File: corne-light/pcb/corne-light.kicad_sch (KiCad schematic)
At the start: 92 parts, among them J1 MJ-4PP-9, J2 OLED, J6 MJ-4PP-9, J7 OLED, SW1 SW_PUSH, SW10 SW_PUSH, SW11 SW_PUSH, SW12 SW_PUSH, SW13 SW_PUSH, SW14 SW_PUSH, SW15 SW_PUSH, SW16 SW_PUSH, SW17 SW_PUSH, SW18 SW_PUSH, SW19 SW_PUSH, SW2 SW_PUSH, SW20 SW_PUSH, SW21 SW_PUSH, SW22 SW_PUSH, SW23 SW_PUSH, SW24 SW_PUSH, SW25 SW_PUSH, SW26 SW_PUSH, SW27 SW_PUSH, SW28 SW_PUSH, SW29 SW_PUSH, SW3 SW_PUSH, SW30 SW_PUSH, SW31 SW_PUSH, SW32 SW_PUSH, SW33 SW_PUSH, SW34 SW_PUSH, SW35 SW_PUSH, SW36 SW_PUSH, SW37 SW_PUSH, SW38 SW_PUSH, SW39 SW_PUSH, SW4 SW_PUSH, SW40 SW_PUSH, SW41 SW_PUSH, SW42 SW_PUSH, SW5 SW_PUSH, SW6 SW_PUSH, SW7 SW_PUSH, SW8 SW_PUSH, SW9 SW_PUSH, U1 ProMicro, U2 ProMicro

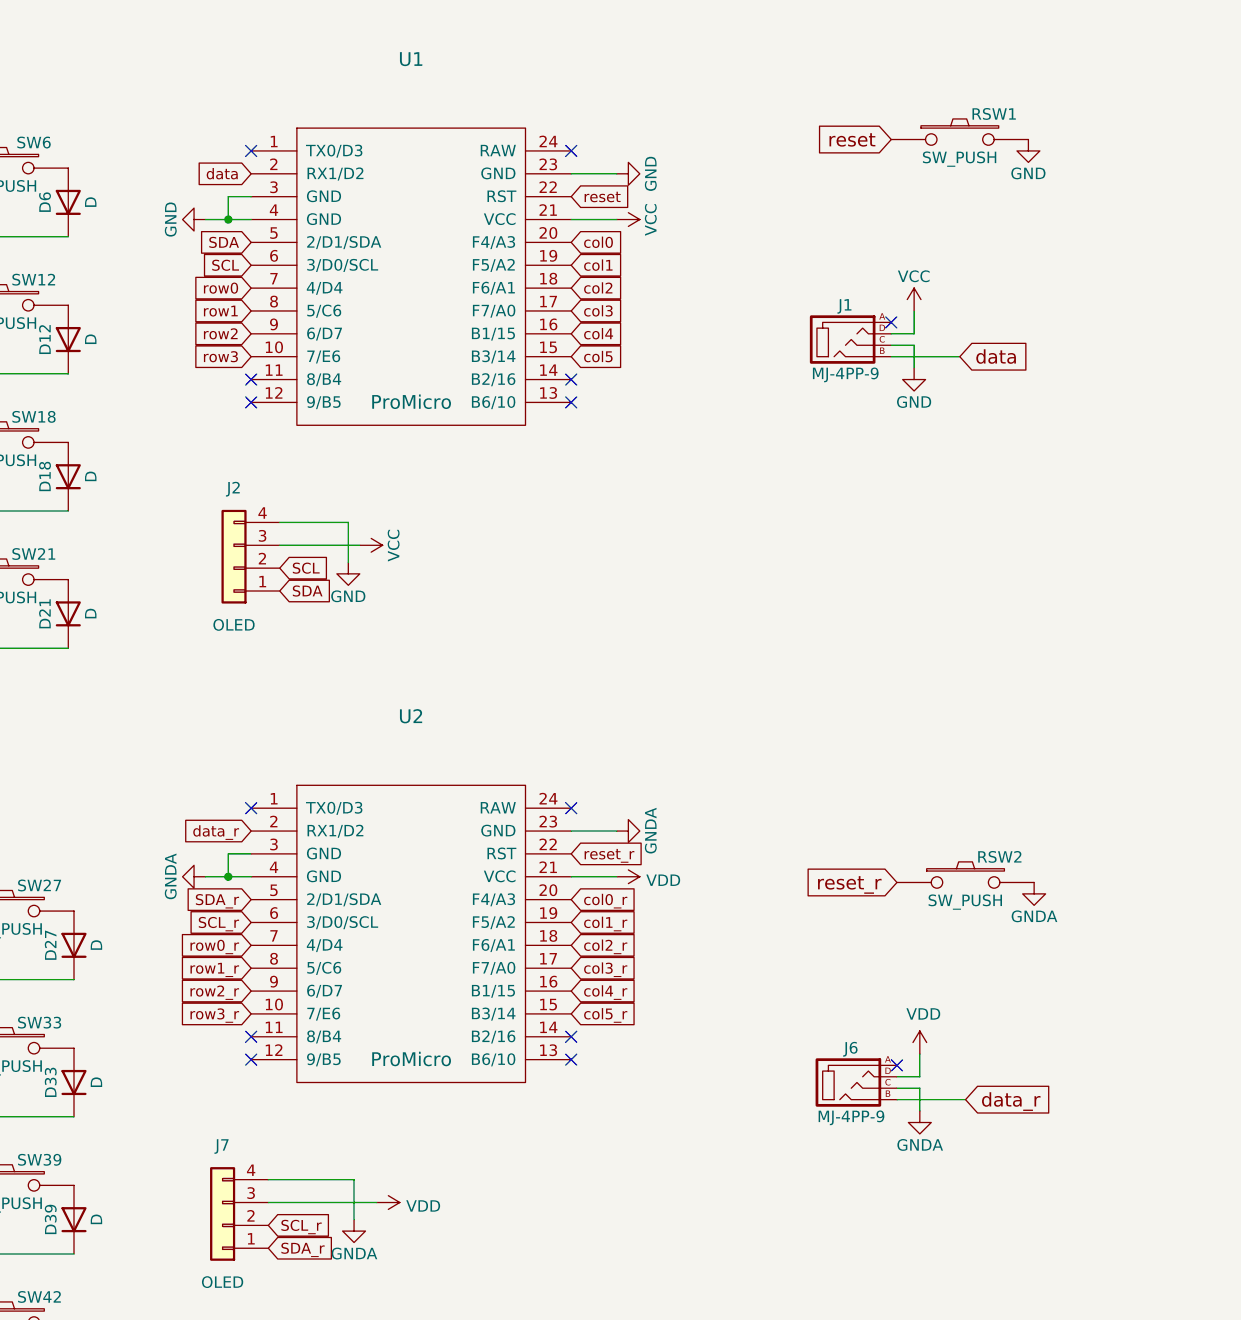
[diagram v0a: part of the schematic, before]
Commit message: Change switches to redragon ones
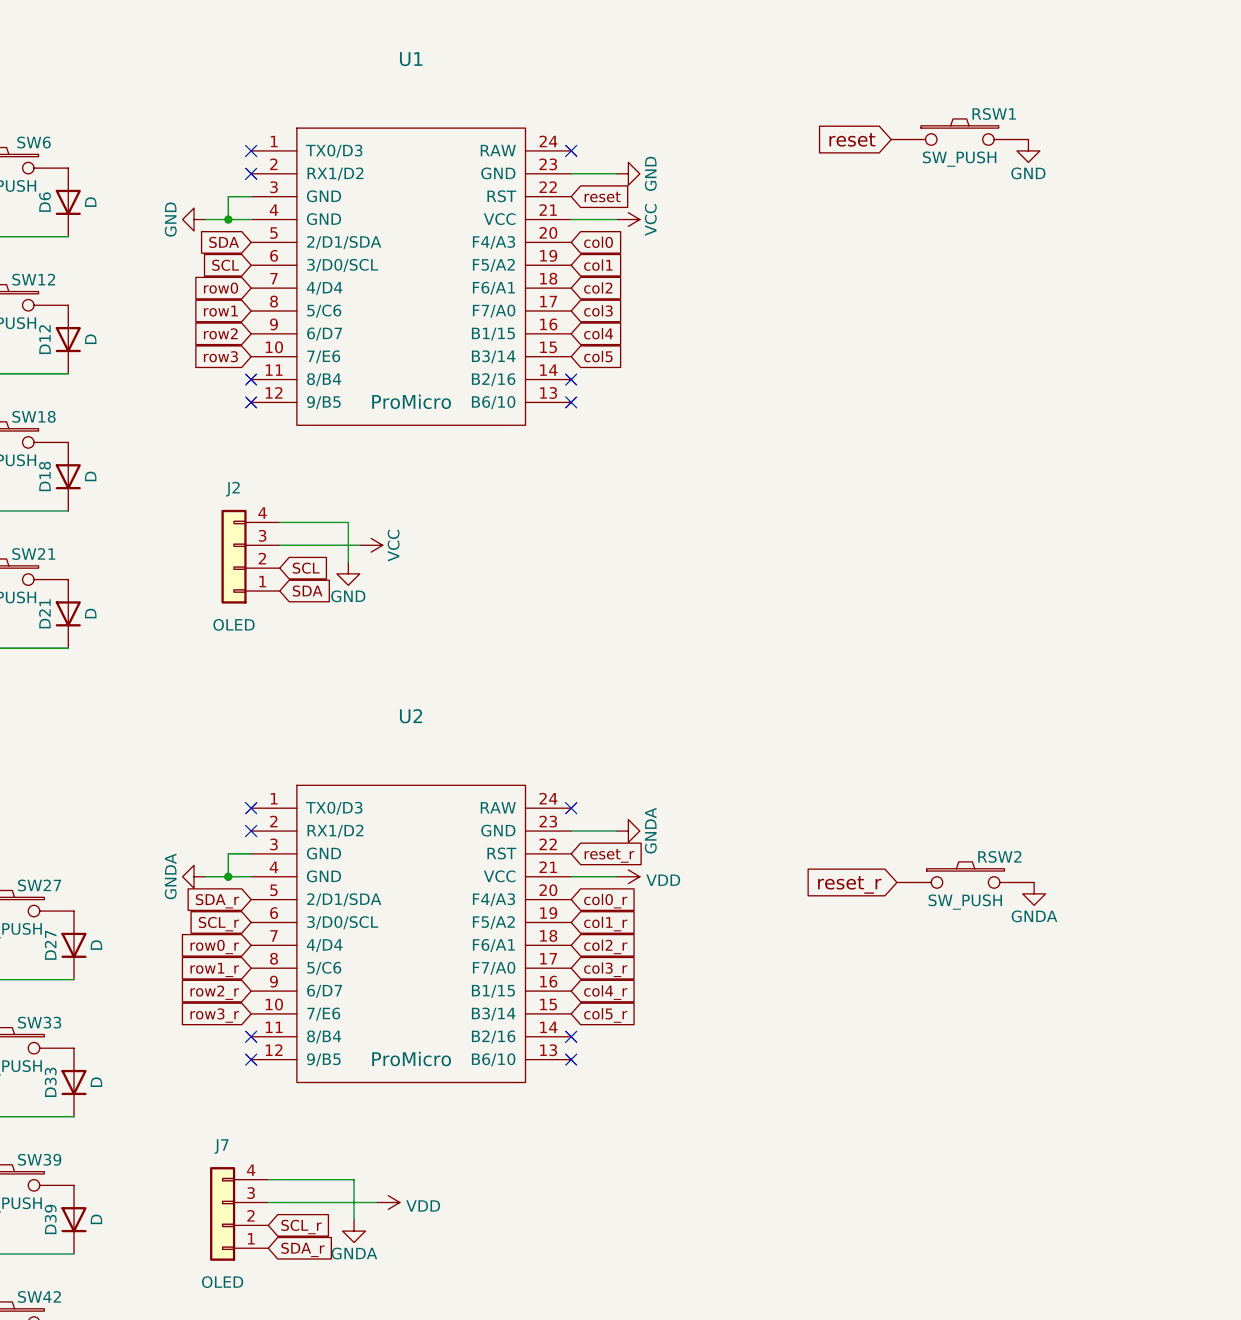
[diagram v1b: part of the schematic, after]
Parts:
- removed J1, J6: MJ-4PP-9, kbd:MJ-4PP-9_1side, symbol kbd:MJ-4PP-9
- SW1, SW10, SW11, SW12, SW13, SW14, SW15, SW16, SW17, SW18, SW19, SW2, SW20, SW22, SW23, SW24, SW25, SW26, SW27, SW28, SW29, SW3, SW30, SW31, SW32, SW33, SW34, SW35, SW36, SW37, SW38, SW39, SW4, SW40, SW41, SW5, SW6, SW7, SW8, SW9: footprint kbd:CherryMX_ChocV2_1u -> ProjectLocal:SW_Redragon_LowProfile_PCB_1.00u
- SW21, SW42: footprint kbd:CherryMX_ChocV2_1.5u -> ProjectLocal:SW_Redragon_LowProfile_PCB_1.50u
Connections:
- net data: no longer names the net of U1.2 (RX1/D2)
- net data_r: no longer names the net of U2.2 (RX1/D2)

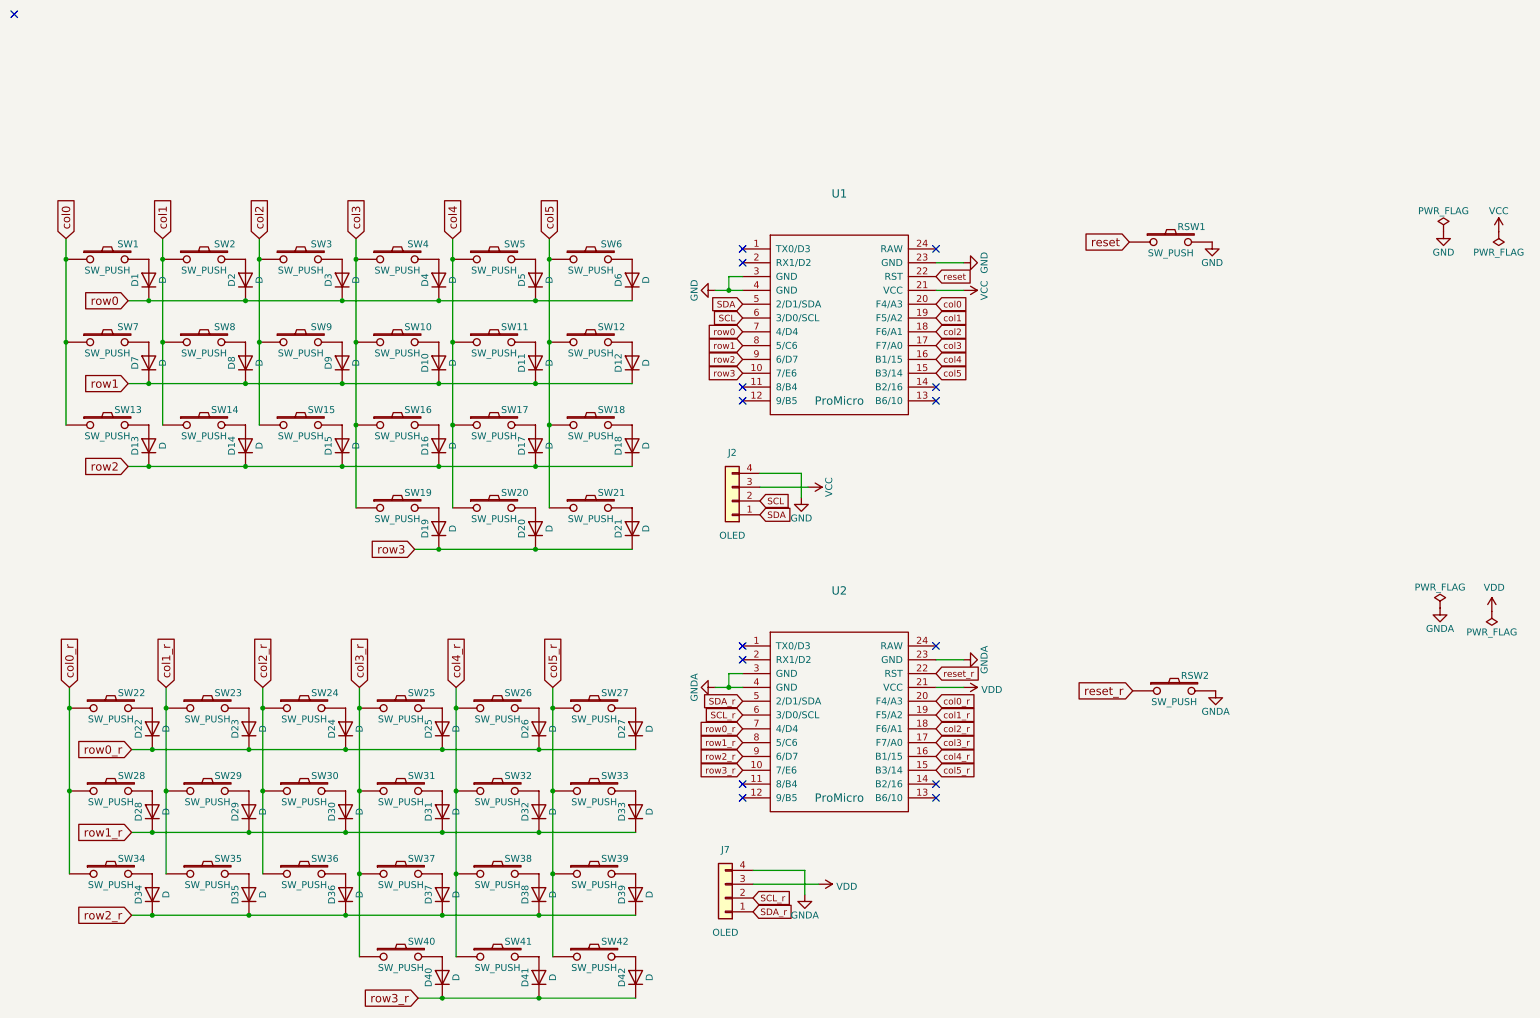
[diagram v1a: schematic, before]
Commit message: Change diode orientation on right side
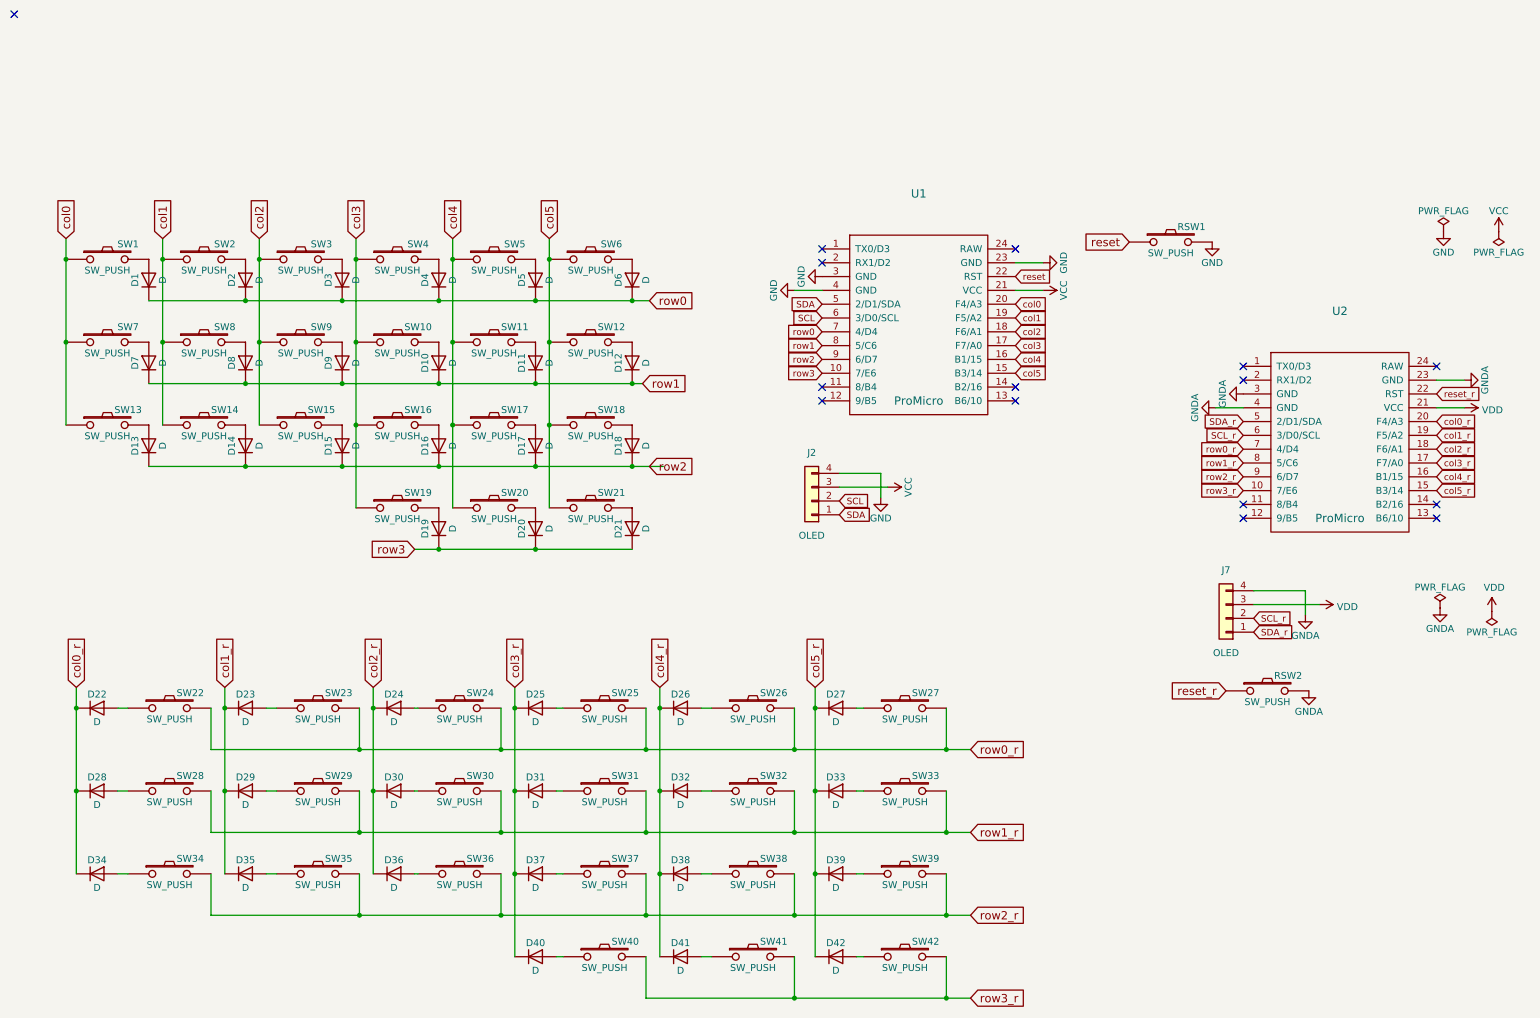
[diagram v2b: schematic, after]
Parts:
- D1, D10, D11, D12, D13, D14, D15, D16, D17, D18, D19, D2, D20, D21, D22, D23, D24, D25, D26, D27, D28, D29, D3, D30, D31, D32, D33, D34, D35, D36, D37, D38, D39, D4, D40, D41, D42, D5, D6, D7, D8, D9: footprint kbd:D3_TH -> Diode_THT:D_DO-35_SOD27_P12.70mm_Horizontal
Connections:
- net col0_r: now also D22.1 (K), D28.1 (K), D34.1 (K); no longer SW22.1, SW28.1, SW34.1
- net col1_r: now also D23.1 (K), D29.1 (K), D35.1 (K); no longer SW23.1, SW29.1, SW35.1
- net col2_r: now also D24.1 (K), D30.1 (K), D36.1 (K); no longer SW24.1, SW30.1, SW36.1
- net col3_r: now also D25.1 (K), D31.1 (K), D37.1 (K), D40.1 (K); no longer SW25.1, SW31.1, SW37.1, SW40.1
- net col4_r: now also D26.1 (K), D32.1 (K), D38.1 (K), D41.1 (K); no longer SW26.1, SW32.1, SW38.1, SW41.1
- net col5_r: now also D27.1 (K), D33.1 (K), D39.1 (K), D42.1 (K); no longer SW27.1, SW33.1, SW39.1, SW42.1
- net row0_r: now also SW22.2, SW23.2, SW24.2, SW25.2, SW26.2, SW27.2; no longer D22.1 (K), D23.1 (K), D24.1 (K), D25.1 (K), D26.1 (K), D27.1 (K)
- net row1_r: now also SW28.2, SW29.2, SW30.2, SW31.2, SW32.2, SW33.2; no longer D28.1 (K), D29.1 (K), D30.1 (K), D31.1 (K), D32.1 (K), D33.1 (K)
- net row2_r: now also SW34.2, SW35.2, SW36.2, SW37.2, SW38.2, SW39.2; no longer D34.1 (K), D35.1 (K), D36.1 (K), D37.1 (K), D38.1 (K), D39.1 (K)
- net row3_r: now also SW40.2, SW41.2, SW42.2; no longer D40.1 (K), D41.1 (K), D42.1 (K)
- net at D23.2 (A): now also SW23.1; no longer SW23.2
- net at D24.2 (A): now also SW24.1; no longer SW24.2
- net at D25.2 (A): now also SW25.1; no longer SW25.2
- net at D26.2 (A): now also SW26.1; no longer SW26.2
- net at D27.2 (A): now also SW27.1; no longer SW27.2
- net at D22.2 (A): now also SW22.1; no longer SW22.2
- net at D29.2 (A): now also SW29.1; no longer SW29.2
- net at D30.2 (A): now also SW30.1; no longer SW30.2
- net at D31.2 (A): now also SW31.1; no longer SW31.2
- net at D32.2 (A): now also SW32.1; no longer SW32.2
- net at D33.2 (A): now also SW33.1; no longer SW33.2
- net at D28.2 (A): now also SW28.1; no longer SW28.2
- net at D35.2 (A): now also SW35.1; no longer SW35.2
- net at D36.2 (A): now also SW36.1; no longer SW36.2
- net at D37.2 (A): now also SW37.1; no longer SW37.2
- net at D38.2 (A): now also SW38.1; no longer SW38.2
- net at D39.2 (A): now also SW39.1; no longer SW39.2
- net at D34.2 (A): now also SW34.1; no longer SW34.2
- net at D41.2 (A): now also SW41.1; no longer SW41.2
- net at D42.2 (A): now also SW42.1; no longer SW42.2
- net at D40.2 (A): now also SW40.1; no longer SW40.2
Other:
- moved on the sheet: D22, D23, D24, D25, D26, D27, D28, D29, D30, D31, D32, D33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

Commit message: Route rightside keys
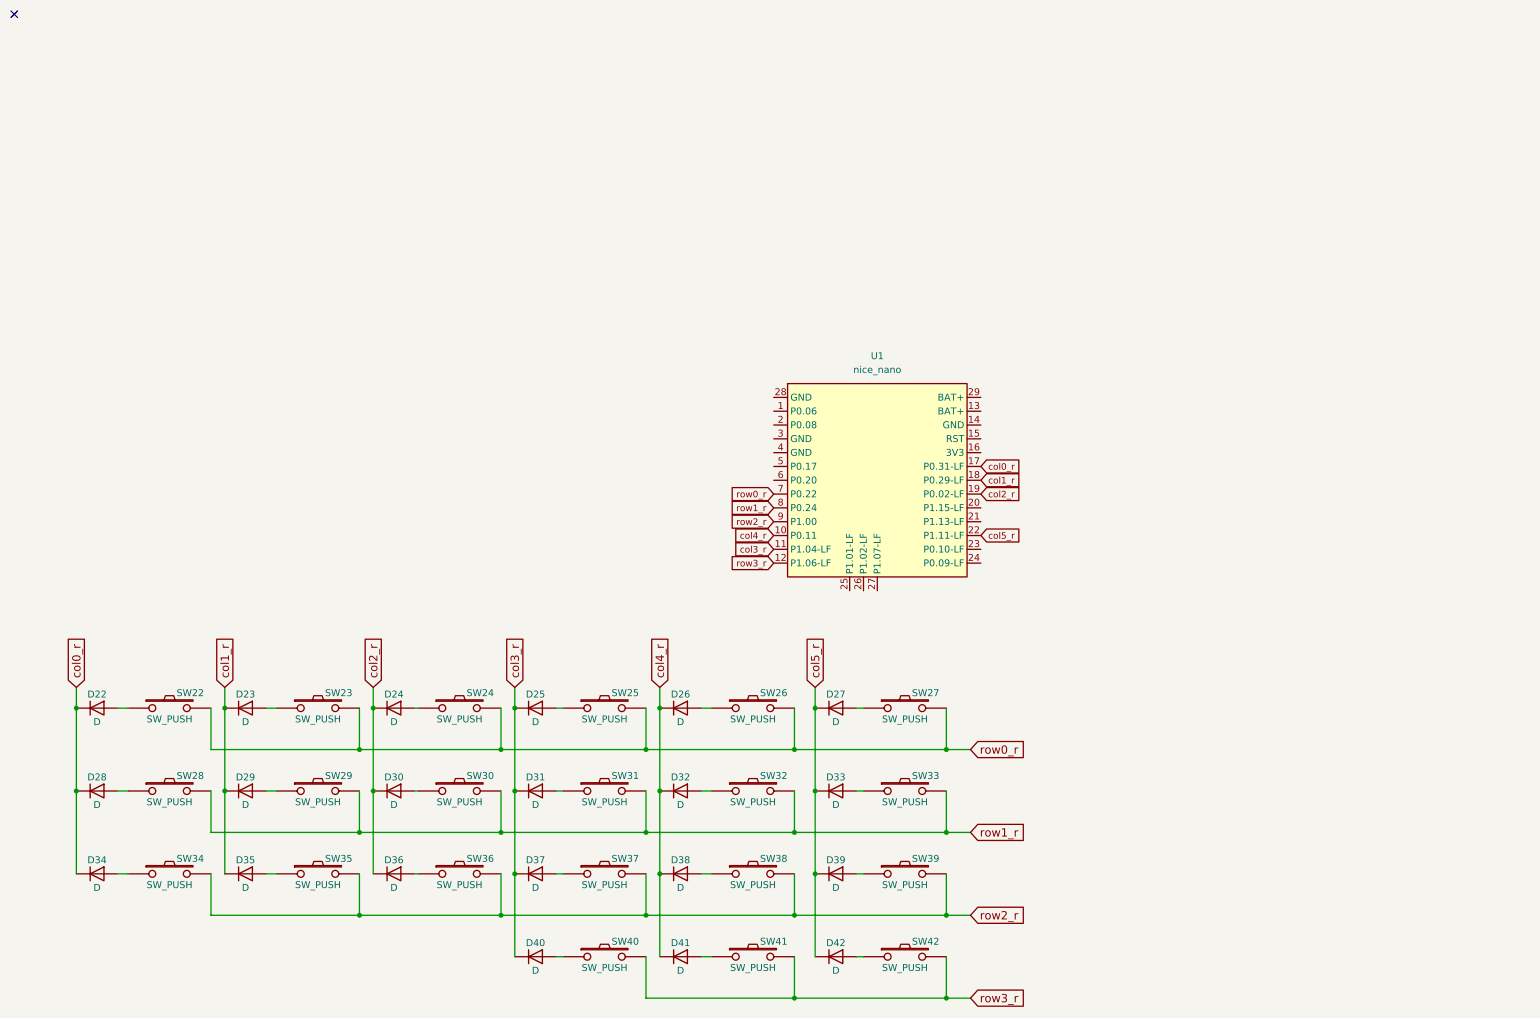
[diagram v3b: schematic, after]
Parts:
- removed D1, D10, D11, D12, D13, D14, D15, D16, D17, D18, D19, D2, D20, D21, D3, D4, D5, D6, D7, D8, D9: D, Diode_THT:D_DO-35_SOD27_P12.70mm_Horizontal, symbol Device:D
- removed J2, J7: OLED, kbd:OLED_1side, symbol Connector_Generic:Conn_01x04
- removed RSW1, RSW2: SW_PUSH, kbd:ResetSW_1side, symbol kbd:SW_PUSH
- removed SW1, SW10, SW11, SW12, SW13, SW14, SW15, SW16, SW17, SW18, SW19, SW2, SW20, SW3, SW4, SW5, SW6, SW7, SW8, SW9: SW_PUSH, ProjectLocal:SW_Redragon_LowProfile_PCB_1.00u, symbol kbd:SW_PUSH
- removed SW21: SW_PUSH, ProjectLocal:SW_Redragon_LowProfile_PCB_1.50u, symbol kbd:SW_PUSH
- removed U1, U2: ProMicro, kbd:ProMicro_v3, symbol kbd:ProMicro
- added U1: nice_nano, PCM_marbastlib-xp-promicroish:nice_nano_AH_USBup, symbol PCM_marbastlib-promicroish:nice_nano
- D22, D23, D24, D25, D26, D27, D28, D29, D30, D31, D32, D33, D34, D35, D36, D37, D38, D39, D40, D41, D42: footprint Diode_THT:D_DO-35_SOD27_P12.70mm_Horizontal -> Diode_THT:D_DO-35_SOD27_P10.16mm_Horizontal
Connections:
- net col0_r: now also U1.17 (P0.31-LF)
- net col1_r: now also U1.18 (P0.29-LF)
- net col2_r: now also U1.19 (P0.02-LF)
- net col3_r: now also U1.11 (P1.04-LF)
- net col4_r: now also U1.10 (P0.11)
- net col5_r: now also U1.22 (P1.11-LF)
- net row0_r: now also U1.7 (P0.22)
- net row1_r: now also U1.8 (P0.24)
- net row2_r: now also U1.9 (P1.00)
- net row3_r: now also U1.12 (P1.06-LF)
- no-connect marks 15 -> 1
